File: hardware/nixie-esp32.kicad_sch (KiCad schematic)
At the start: 15 parts, among them J1 USB4216-03-A_REVA, SW1 RESET, SW2 BOOT, U1 AP7361C-33E-13, U2 ESP32-S3-WROOM-1

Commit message: Progress point
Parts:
- C1, C2: footprint (none) -> Capacitor_SMD:C_1206_3216Metric
- C3: footprint (none) -> Capacitor_SMD:C_0805_2012Metric
- D1: footprint SOT50P160X60-5N -> nixie-esp32:SOT50P160X60-5N
- J1: footprint USB4216-03-A_REVA:GCT_USB4216-03-A_REVA -> nixie-esp32:GCT_USB4216-03-A_REVA
- R1, R2, R6: footprint (none) -> Resistor_SMD:R_0805_2012Metric
- R3: renamed from R5; footprint (none) -> Resistor_SMD:R_0805_2012Metric
- R4: renamed from R3; footprint (none) -> Resistor_SMD:R_0805_2012Metric
- R5: renamed from R4; footprint (none) -> Resistor_SMD:R_0805_2012Metric
- U1: footprint SOT223_DIO -> nixie-esp32:SOT223_DIO
- U2: footprint PCM_Espressif:ESP32-S3-WROOM-1 -> nixie-esp32:ESP32-S3-WROOM-1
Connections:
- net GND: now also J1.SH1 (SHIELD), J1.SH2 (SHIELD), J1.SH3 (SHIELD), J1.SH4 (SHIELD)
- net ESP32_GPIO8: now reaches U2.12 (GPIO8/TOUCH8/ADC1_CH7/SUBSPICS1)
- net ESP32_GPIO9: now reaches U2.17 (GPIO9/TOUCH9/ADC1_CH8/FSPIHD/SUBSPIHD)
- net ESP32_GPIO10: now reaches U2.18 (GPIO10/TOUCH10/ADC1_CH9/FSPICS0/FSPIIO4/SUBSPICS0)
- net ESP32_GPIO11: now reaches U2.19 (GPIO11/TOUCH11/ADC2_CH0/FSPID/FSPIIO5/SUBSPID)
- no-connect marks 4 -> 32
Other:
- added sheet Nixies (nixies.kicad_sch)

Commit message: Lock in PTS645SL70SMTR92_LFS as the tactile BOOT/RESET buttons
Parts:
- SW1, SW2: footprint (none) -> nixie-esp32:PTS645SL70SMTR92LFS; symbol Switch:SW_Push -> nixie-esp32:PTS645SL70SMTR92_LFS; Manufacturer (none) -> C&K; Manufacturer_Part_Number (none) -> PTS645SL70SMTR92 LFS
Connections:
- net GND: now also SW1.3 (COM_1), SW1.4 (COM_2), SW2.3 (COM_1), SW2.4 (COM_2); no longer SW1.1, SW2.1
- net at R6.2, SW2.2 (NO_2), U2.27 (GPIO0/BOOT): now also SW2.1 (NO_1)
- net at R3.2, SW1.2 (NO_2), U2.3 (EN): now also SW1.1 (NO_1)
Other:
- moved on the sheet: R6

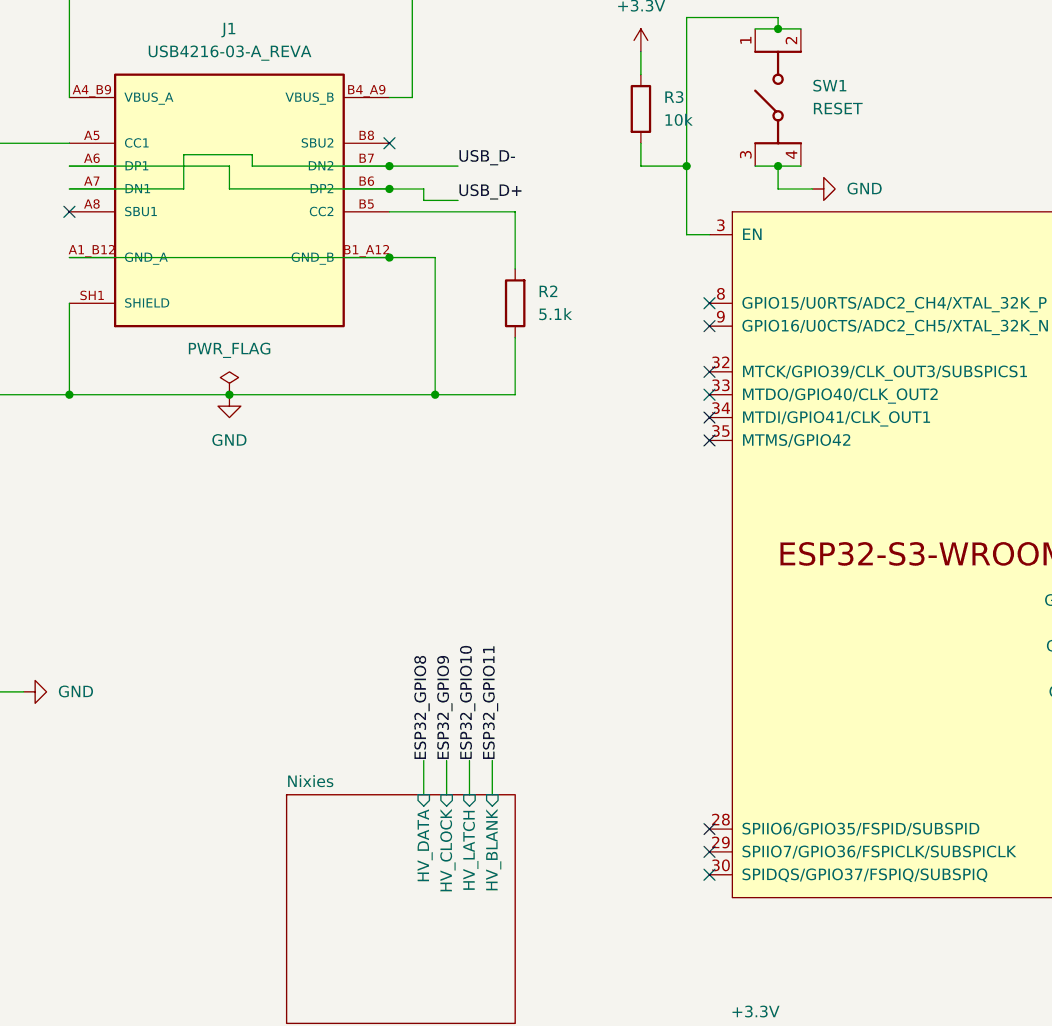
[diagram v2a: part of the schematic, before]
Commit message: Address schematic audit findings
- Move C15 to the ESP32 EN node for proper power-on RC delay and button reset
- Add 10k boot-glitch pull-downs (R13-R16) on the CD4504 level shifter inputs
- Add NCH8200HV input capacitor (C16)
- Switch D2-D4 to the Bivar SMTLA5050RGB symbol/footprint
- Label nixie anode nets and add HV net class with custom DRC clearance rules
- Normalize value formats and assign missing footprints
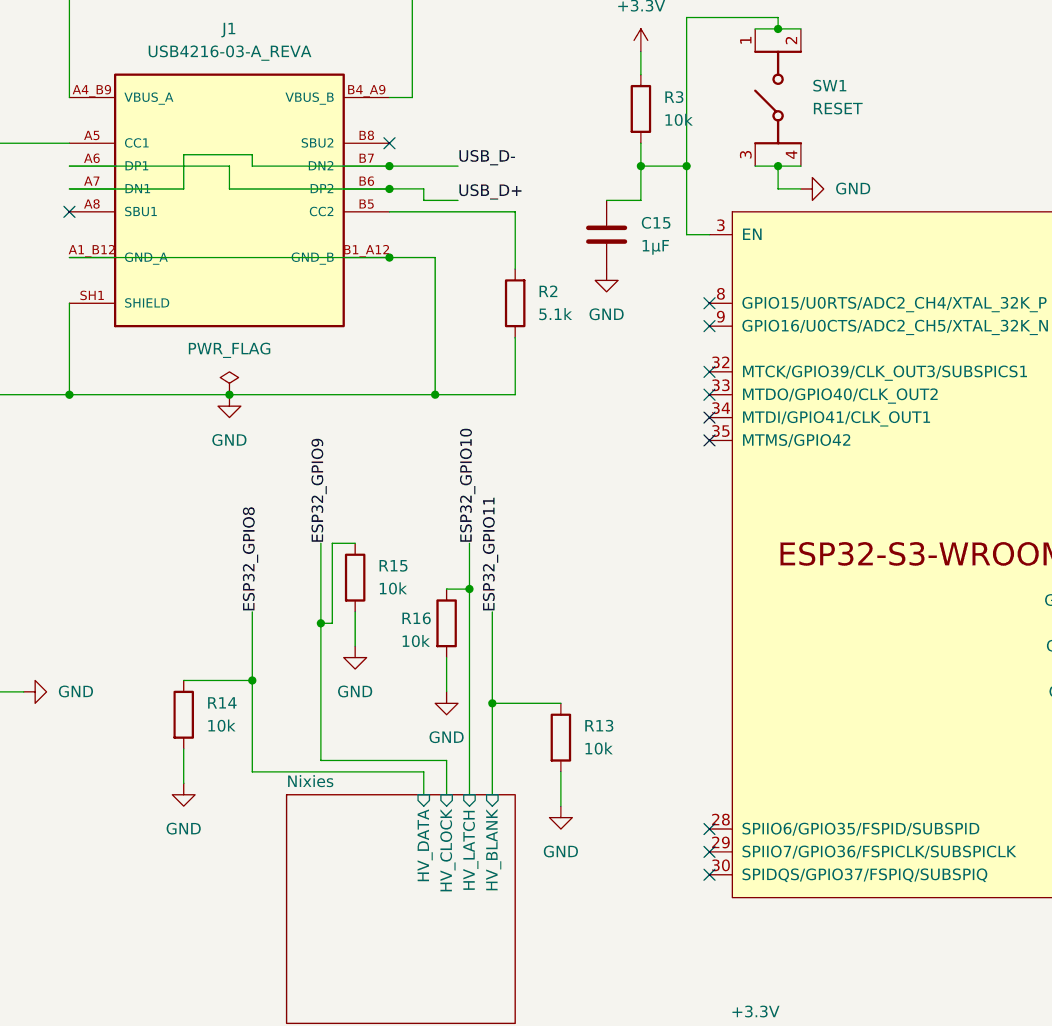
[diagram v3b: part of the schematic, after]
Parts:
- added C15: 1µF, Capacitor_SMD:C_0805_2012Metric, symbol Device:C
- added R13, R14, R15, R16: 10k, Resistor_SMD:R_0805_2012Metric, symbol Device:R
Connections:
- net ESP32_GPIO10: now also R16.1
- net ESP32_GPIO11: now also R13.1
- net ESP32_GPIO8: now also R14.1
- net ESP32_GPIO9: now also R15.1
- net GND: now also C15.2, R13.2, R14.2, R15.2, R16.2
- net at R3.2, SW1.1 (NO_1), SW1.2 (NO_2)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: now also C15.1
